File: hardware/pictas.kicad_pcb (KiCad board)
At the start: 2 copper layers, 57.2 x 71.1 mm, 22 parts, among them Y1 Crystal

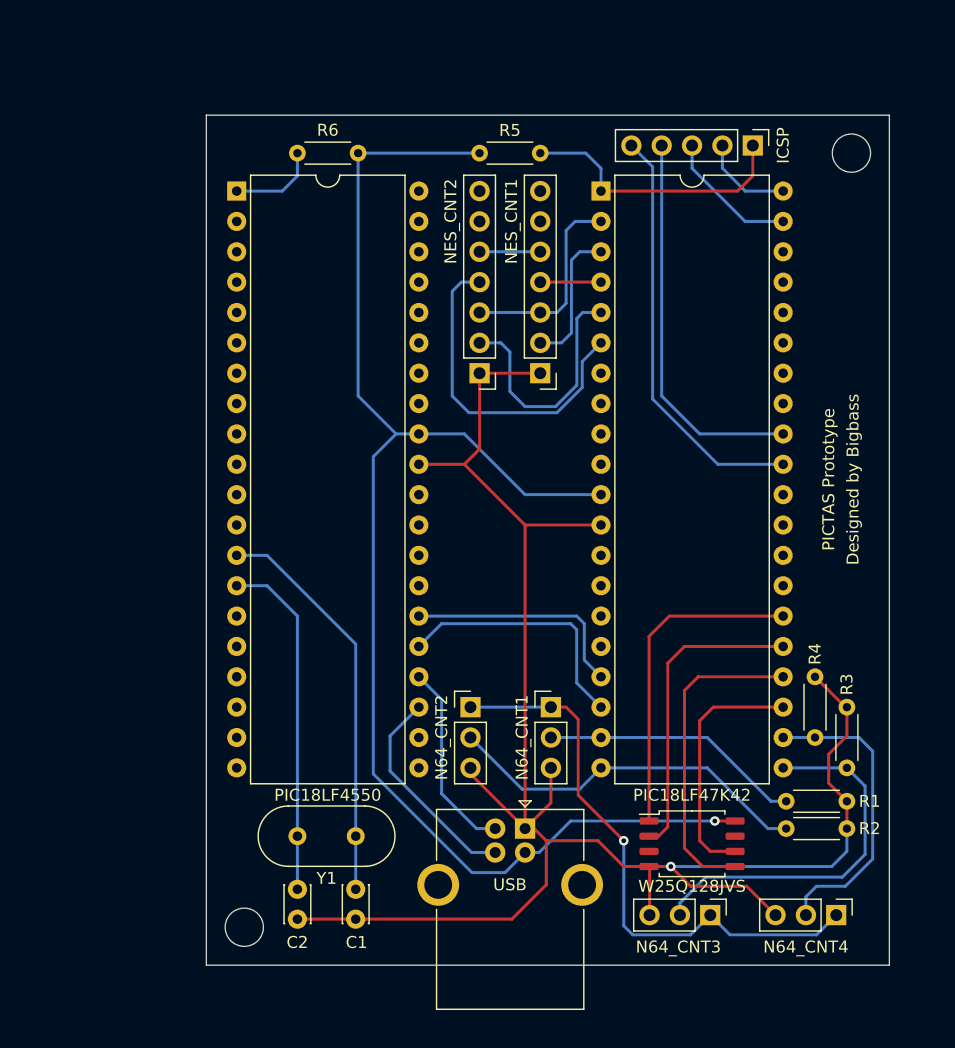
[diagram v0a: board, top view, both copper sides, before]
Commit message: Redesigned PCB. Better controller placement and added visualization board connectors.
Signed-off-by: bigbass1997 <bigbass1997.website@gmail.com>
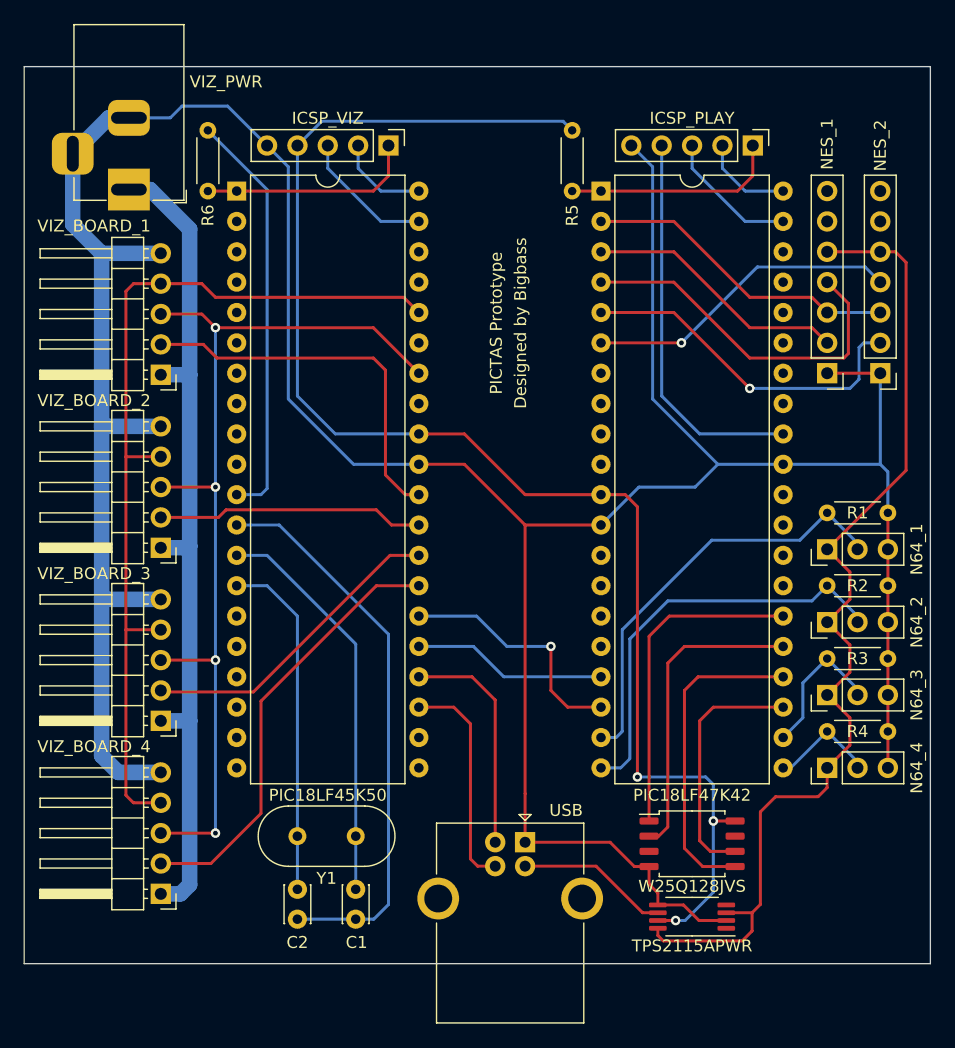
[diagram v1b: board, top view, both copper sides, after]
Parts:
- removed ICSP: ICSP, Connector_PinHeader_2.54mm:PinHeader_1x05_P2.54mm_Vertical
- removed N64_CNT1: N64_CNT1, Connector_PinHeader_2.54mm:PinHeader_1x03_P2.54mm_Vertical
- removed N64_CNT2: N64_CNT2, Connector_PinHeader_2.54mm:PinHeader_1x03_P2.54mm_Vertical
- removed N64_CNT3: N64_CNT3, Connector_PinHeader_2.54mm:PinHeader_1x03_P2.54mm_Vertical
- removed N64_CNT4: N64_CNT4, Connector_PinHeader_2.54mm:PinHeader_1x03_P2.54mm_Vertical
- removed NES_CNT1: NES_CNT1, Connector_PinHeader_2.54mm:PinHeader_1x07_P2.54mm_Vertical
- removed NES_CNT2: NES_CNT2, Connector_PinHeader_2.54mm:PinHeader_1x07_P2.54mm_Vertical
- removed PIC18LF4550: PIC18LF4550-IP-PinAligned, Package_DIP:DIP-40_W15.24mm
- removed REF** (x2): MountingHole_3.2mm_M3_DIN965, MountingHole:MountingHole_3.2mm_M3_DIN965
- added ICSP_PLAY: ICSP_PLAY, Connector_PinHeader_2.54mm:PinHeader_1x05_P2.54mm_Vertical, F.Cu at (117.5, 61.0)
- added ICSP_VIZ: ICSP_VIZ, Connector_PinHeader_2.54mm:PinHeader_1x05_P2.54mm_Vertical, F.Cu at (87.0, 61.0)
- added N64_1: N64_CNT1, Connector_PinHeader_2.54mm:PinHeader_1x03_P2.54mm_Vertical, F.Cu at (123.7, 94.7)
- added N64_2: N64_CNT2, Connector_PinHeader_2.54mm:PinHeader_1x03_P2.54mm_Vertical, F.Cu at (123.7, 100.8)
- added N64_3: N64_CNT3, Connector_PinHeader_2.54mm:PinHeader_1x03_P2.54mm_Vertical, F.Cu at (123.7, 106.9)
- added N64_4: N64_CNT4, Connector_PinHeader_2.54mm:PinHeader_1x03_P2.54mm_Vertical, F.Cu at (123.7, 113.0)
- added NES_1: NES_CNT1, Connector_PinHeader_2.54mm:PinHeader_1x07_P2.54mm_Vertical, F.Cu at (123.7, 80.0)
- added NES_2: NES_CNT2, Connector_PinHeader_2.54mm:PinHeader_1x07_P2.54mm_Vertical, F.Cu at (128.1, 80.0)
- added PIC18LF45K50: PIC18LF45K50, Package_DIP:DIP-40_W15.24mm, F.Cu at (74.3, 64.8)
- added TPS2115APWR: TPS2115APWR, Package_SO:TSSOP-8_4.4x3mm_P0.65mm, F.Cu at (112.4, 125.5)
- added VIZ_BOARD_1: VizBoard0, Connector_PinHeader_2.54mm:PinHeader_1x05_P2.54mm_Horizontal, F.Cu at (67.9, 80.1)
- added VIZ_BOARD_2: VizBoard1, Connector_PinHeader_2.54mm:PinHeader_1x05_P2.54mm_Horizontal, F.Cu at (67.9, 94.6)
- added VIZ_BOARD_3: VizBoard2, Connector_PinHeader_2.54mm:PinHeader_1x05_P2.54mm_Horizontal, F.Cu at (67.9, 109.1)
- added VIZ_BOARD_4: VizBoard3, Connector_PinHeader_2.54mm:PinHeader_1x05_P2.54mm_Horizontal, F.Cu at (67.9, 123.6)
- added VIZ_PWR: LED_Power_Jack, Connector_BarrelJack:BarrelJack_Horizontal, F.Cu at (65.3, 64.6)
- C1, C2: value C -> 27pF
- W25Q128JVS: value W25Q128JVS -> W25Q128JVS_PinAligned
- Y1: value Crystal -> 16MHz
- moved R1 24.4 mm to (128.8, 91.7)
- moved R2 20.6 mm to (128.8, 97.8)
- moved R6 8.14 mm to (71.9, 64.8), turned to 90 degrees
- moved R4 7.62 mm to (128.8, 110.0), turned to 180 degrees
- moved R3 5.32 mm to (128.8, 103.9), turned to 180 degrees
- moved R5 4.15 mm to (102.4, 64.8), turned to 90 degrees
- moved USB 1.14 mm to (98.4, 119.3)
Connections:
- C1 pad 2: /GND -> Net-(C1-Pad2)
- C2 pad 2: /GND -> Net-(C1-Pad2)
- PIC18LF47K42 pad 11: /USB_5V -> /Power Select/OUT_PWR
- PIC18LF47K42 pad 17: /U1RX -> /-->UART
- PIC18LF47K42 pad 18: /U1TX -> /<--UART
- PIC18LF47K42 pad 21: /N64_DATA3 -> /N64_DATA4
- PIC18LF47K42 pad 22: /N64_DATA4 -> /N64_DATA3
- PIC18LF47K42 pad 31: Net-(J7-Pad5) -> /GND
- R5 pad 2: /USB_5V -> /Power Select/OUT_PWR
- R6 pad 2: /USB_5V -> Net-(R6-Pad2)
- W25Q128JVS pad 8: /USB_5V -> /Power Select/OUT_PWR
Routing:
- net /GND: track 155.8 -> 283.9 mm, vias 1 -> 0
- net /Power Select/OUT_PWR: track 0.00 -> 123.1 mm, vias 0 -> 3
- net /USB_5V: track 118.9 -> 12.7 mm, vias 1 -> 0
- net /CLK: track 0.00 -> 79.6 mm, vias 0 -> 4
- net /SER: track 0.00 -> 77.0 mm
- net /5V: track 0.00 -> 71.3 mm
- net Net-(C1-Pad2): track 0.00 -> 47.2 mm
- net /3.3V: track 48.4 -> 86.2 mm, vias 1 -> 0
- net /STROBE3: track 0.00 -> 36.7 mm
- net Net-(J7-Pad5): track 35.1 -> 0.00 mm
- net Net-(R6-Pad2): track 0.00 -> 34.8 mm
- net /STROBE0: track 0.00 -> 31.9 mm
- net /STROBE2: track 0.00 -> 26.4 mm
- net /NES_DATA1: track 5.08 -> 30.2 mm
- net /STROBE1: track 0.00 -> 22.4 mm
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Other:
- board size 57.2 x 71.1 mm -> 75.8 x 75.1 mm

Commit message: Updated schematic and prototype PCB design.
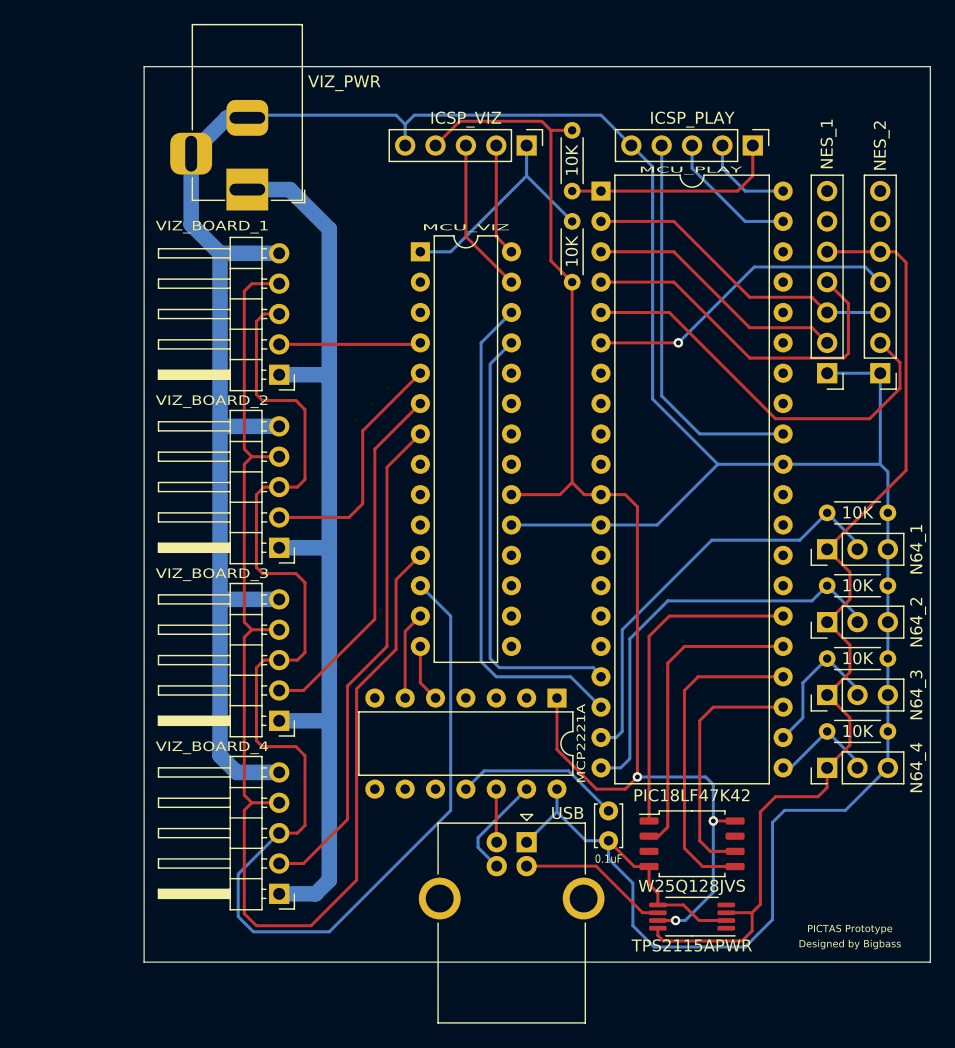
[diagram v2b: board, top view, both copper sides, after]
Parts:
- removed C1, C2: 27pF, Capacitor_THT:C_Disc_D3.0mm_W2.0mm_P2.50mm
- removed PIC18LF45K50: PIC18LF45K50, Package_DIP:DIP-40_W15.24mm
- removed PIC18LF47K42: PIC18LF47K42, Package_DIP:DIP-40_W15.24mm
- removed R6: 10k, Resistor_THT:R_Axial_DIN0204_L3.6mm_D1.6mm_P5.08mm_Horizontal
- removed Y1: 16MHz, Crystal:Crystal_HC49-4H_Vertical
- added 0.1uF: 0.1uF, Capacitor_THT:C_Disc_D3.4mm_W2.1mm_P2.50mm, F.Cu at (105.4, 119.1)
- added 10K: 10K, Resistor_THT:R_Axial_DIN0204_L3.6mm_D1.6mm_P5.08mm_Horizontal, F.Cu at (102.4, 67.3)
- added MCP2221A: MCP2221A, Package_DIP:DIP-14_W7.62mm, F.Cu at (101.1, 107.2)
- added MCU_PLAY: PIC18LF47K42, Package_DIP:DIP-40_W15.24mm, F.Cu at (104.8, 64.8)
- added MCU_VIZ: PIC18F27K42, Package_DIP:DIP-28_W7.62mm, F.Cu at (89.7, 69.8)
- W25Q128JVS: value W25Q128JVS_PinAligned -> W25Q128JVS
- moved ICSP_VIZ 11.6 mm to (98.6, 61.0)
- moved VIZ_BOARD_1 9.91 mm to (77.9, 80.1)
- moved VIZ_BOARD_2 9.91 mm to (77.9, 94.6)
- moved VIZ_BOARD_3 9.91 mm to (77.9, 109.1)
- moved VIZ_BOARD_4 9.91 mm to (77.9, 123.6)
- moved VIZ_PWR 9.91 mm to (75.2, 64.6)
- moved USB 0.13 mm to (98.6, 119.3)
- renumbered R5 to 10K, R4 to 10K, R3 to 10K, R2 to 10K, R1 to 10K
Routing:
- net /UART<--: track 0.00 -> 41.9 mm
- net /UART-->: track 0.00 -> 37.1 mm
- net Net-(R6-Pad2): track 34.8 -> 0.00 mm
- net /CLK: track 79.6 -> 114.1 mm, vias 4 -> 0
- net Net-(C1-Pad1): track 33.6 -> 0.00 mm
- net Net-(C1-Pad2): track 47.2 -> 14.0 mm
- net Net-(C2-Pad1): track 29.0 -> 0.00 mm
- net /SER: track 77.0 -> 104.5 mm
- net /<--UART: track 20.6 -> 0.00 mm, vias 1 -> 0
- net /STROBE0: track 31.9 -> 11.9 mm
- net /-->UART: track 16.3 -> 0.00 mm
- net /D+: track 19.1 -> 4.46 mm
- net /Power Select/OUT_PWR: track 123.1 -> 113.1 mm
- net /D-: track 18.5 -> 8.78 mm
- net /5V: track 71.3 -> 80.1 mm
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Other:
- board size 75.8 x 75.1 mm -> 65.8 x 74.9 mm
